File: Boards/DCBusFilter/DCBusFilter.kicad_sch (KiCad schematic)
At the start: 11 parts, among them J1 TBP01R2-508-04BE

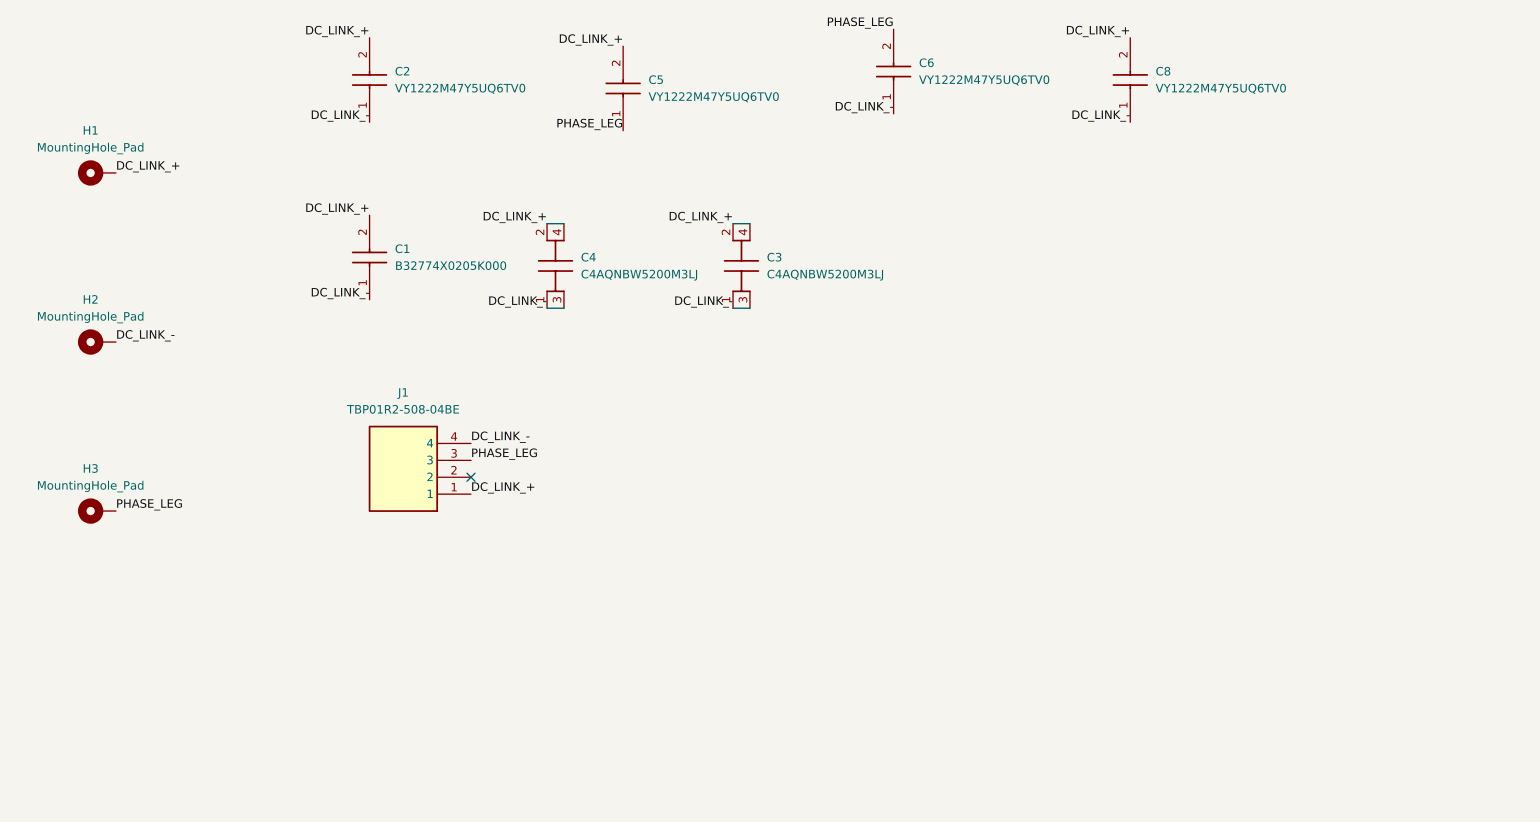
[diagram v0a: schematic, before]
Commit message: add new caps board
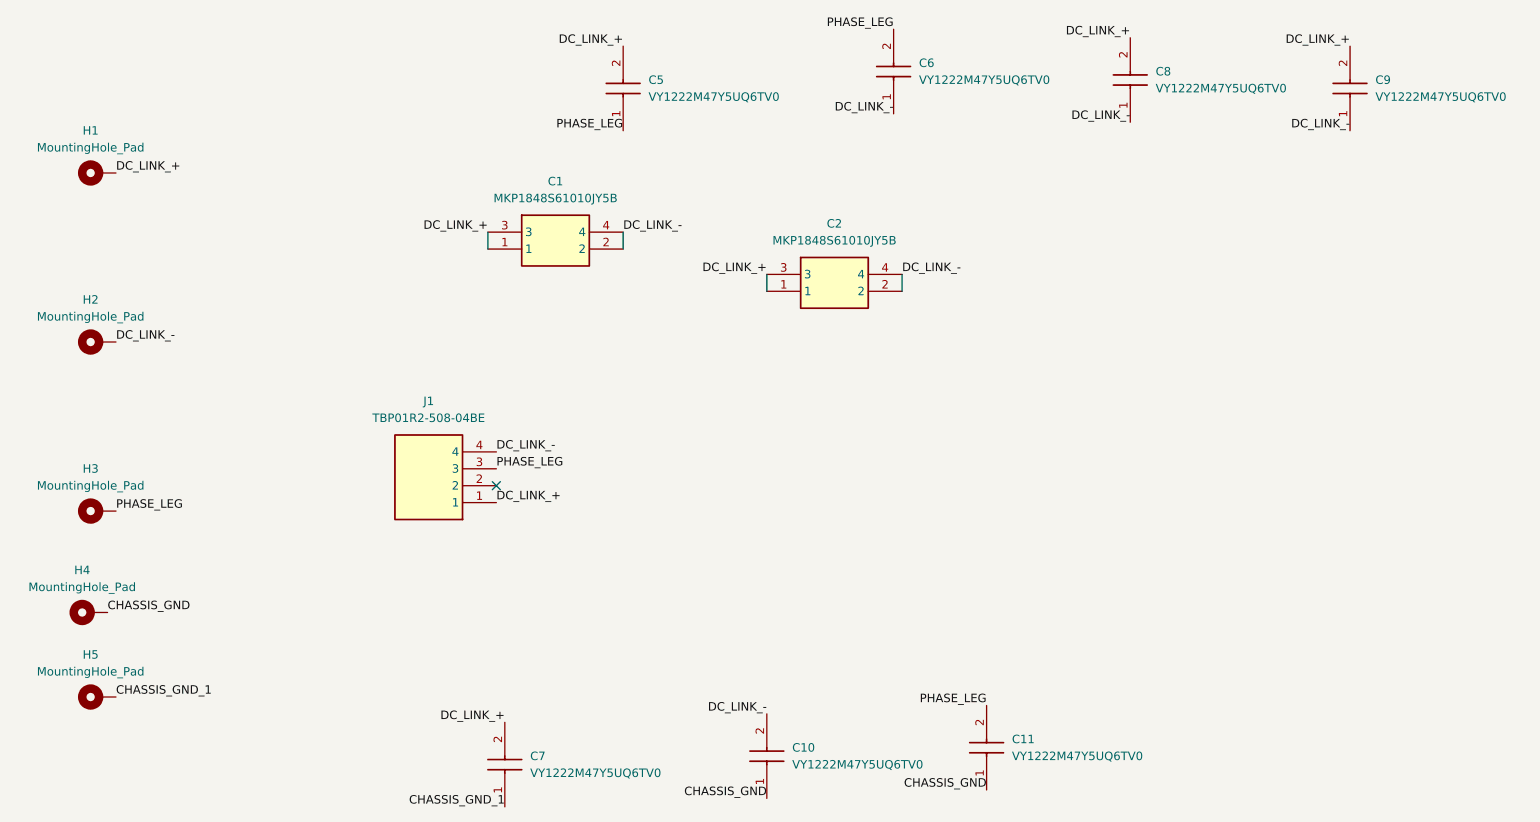
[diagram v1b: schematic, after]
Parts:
- removed C1: B32774X0205K000, InverterCom:B32774X__31.5_x_12.5_, symbol InverterCom:B32774X0205K000
- removed C2: VY1222M47Y5UQ6TV0, VY1222M47Y5UQ6TV0, symbol InverterCom:VY1222M47Y5UQ6TV0
- removed C3, C4: C4AQNBW5200M3LJ, C4AQNBW5200M3LJ, symbol InverterCom:C4AQNBW5200M3LJ
- added C1, C2: MKP1848S61010JY5B, InverterCom:MKP1848S61010JY5B, symbol InverterCom:MKP1848S61010JY5B
- added C10, C11, C7, C9: VY1222M47Y5UQ6TV0, InverterCom:VY1222M47Y5UQ6TV0, symbol InverterCom:VY1222M47Y5UQ6TV0
- added H4, H5: MountingHole_Pad, MountingHole:MountingHole_3.2mm_M3_ISO14580_Pad, symbol Mechanical:MountingHole_Pad
- C5, C6, C8: footprint VY1222M47Y5UQ6TV0 -> InverterCom:VY1222M47Y5UQ6TV0
- J1: footprint SHDR4W100P0X508_1X4_2192X850X1200P -> InverterCom:SHDR4W100P0X508_1X4_2192X850X1200P
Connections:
- net DC_LINK_+: now also C1.1, C1.3, C2.1, C2.3, C7.2, C9.2
- net DC_LINK_-: now also C1.2, C1.4, C10.2, C2.2, C2.4, C9.1
- net PHASE_LEG: now also C11.2
- new net CHASSIS_GND: C10.1, C11.1, H4.1
- new net CHASSIS_GND_1: C7.1, H5.1
